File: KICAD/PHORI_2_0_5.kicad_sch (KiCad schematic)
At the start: 110 parts, among them J1 Conn_01x06_Female, J10 Conn_01x01, J2 Conn_01x02, J3 Rumble, J4 Conn_01x02, J5 Conn_01x06, J6 Conn_01x02, J7 USB-C, J8 Conn_01x06, J9 Conn_01x06, Q1 Q_NMOS_GSD, Q2 Q_PMOS_GDS, Q3 Q_NMOS_GSD, SW1 Z, SW10 Dup, SW11 Dright, SW12 Ddown, SW2 A, SW3 B, SW4 X, SW5 Y, SW6 Start, SW7 L, SW8 R, SW9 Dleft, U1 USB-C-24P-QT, U10 MCP3002, U11 MCP3002, U12 Stickbox_Assembly_CStick, U2 RP2040, U3 W25Q128JVS, U4 DRV5055A2xDBZxQ1, U5 DRV5055A2xDBZxQ1, U6 Stickbox_Assembly_Main, U7 AMS1117-3.3, U8 DRV5055A2xDBZxQ1, U9 DRV5055A2xDBZxQ1, Y1 Crystal_GND24

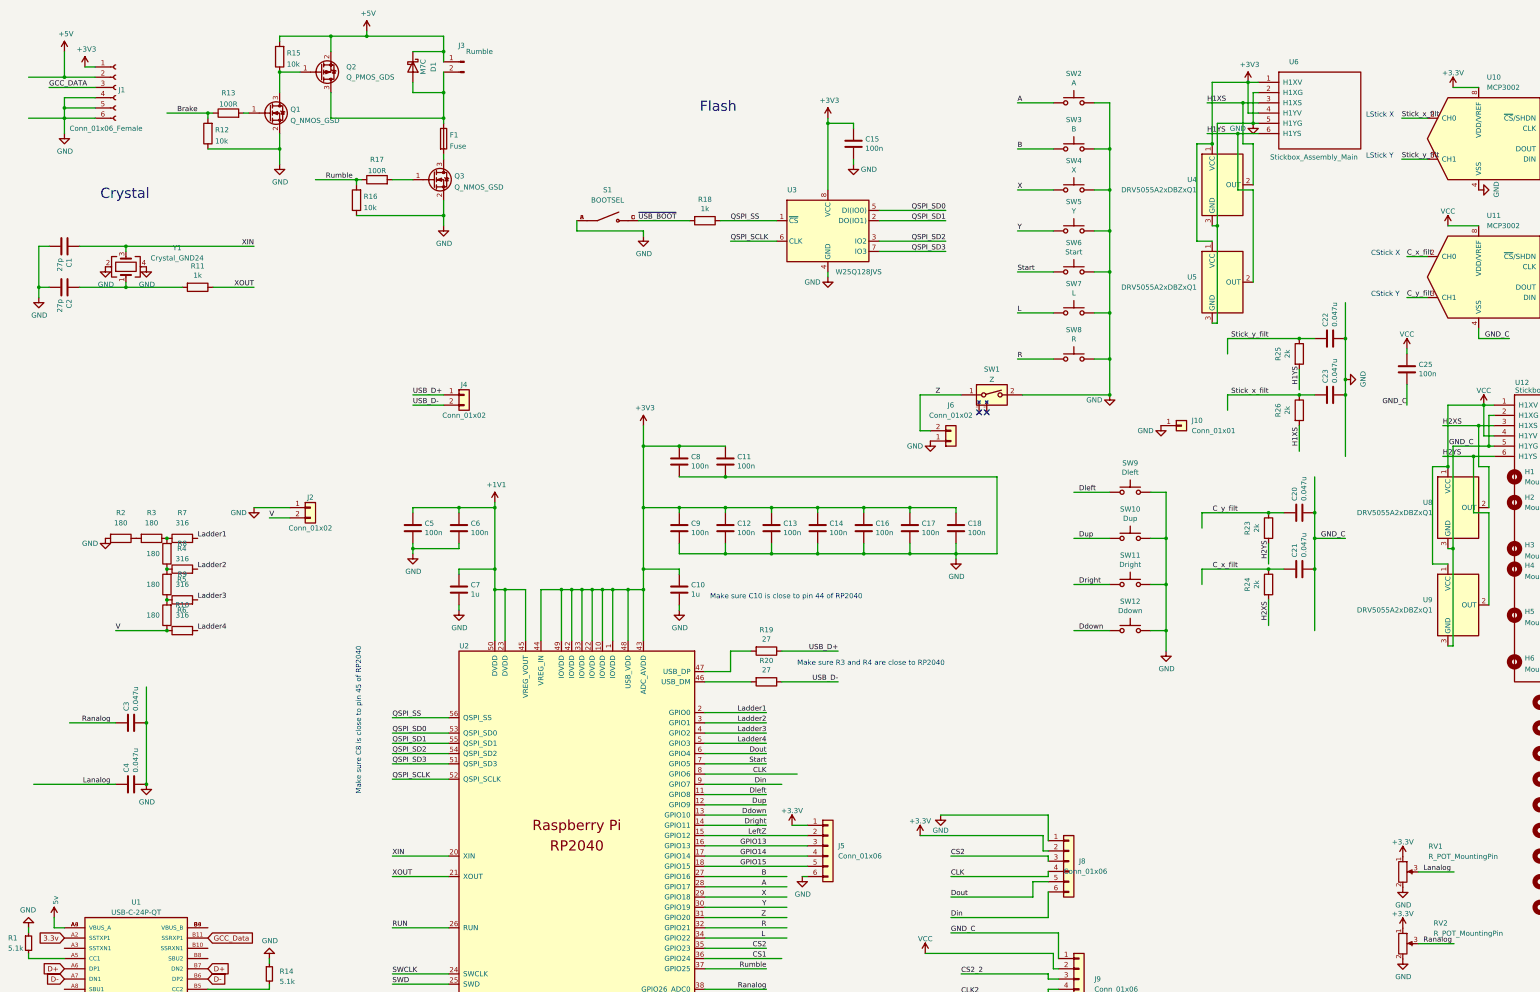
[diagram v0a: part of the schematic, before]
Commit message: GND on Rp2040
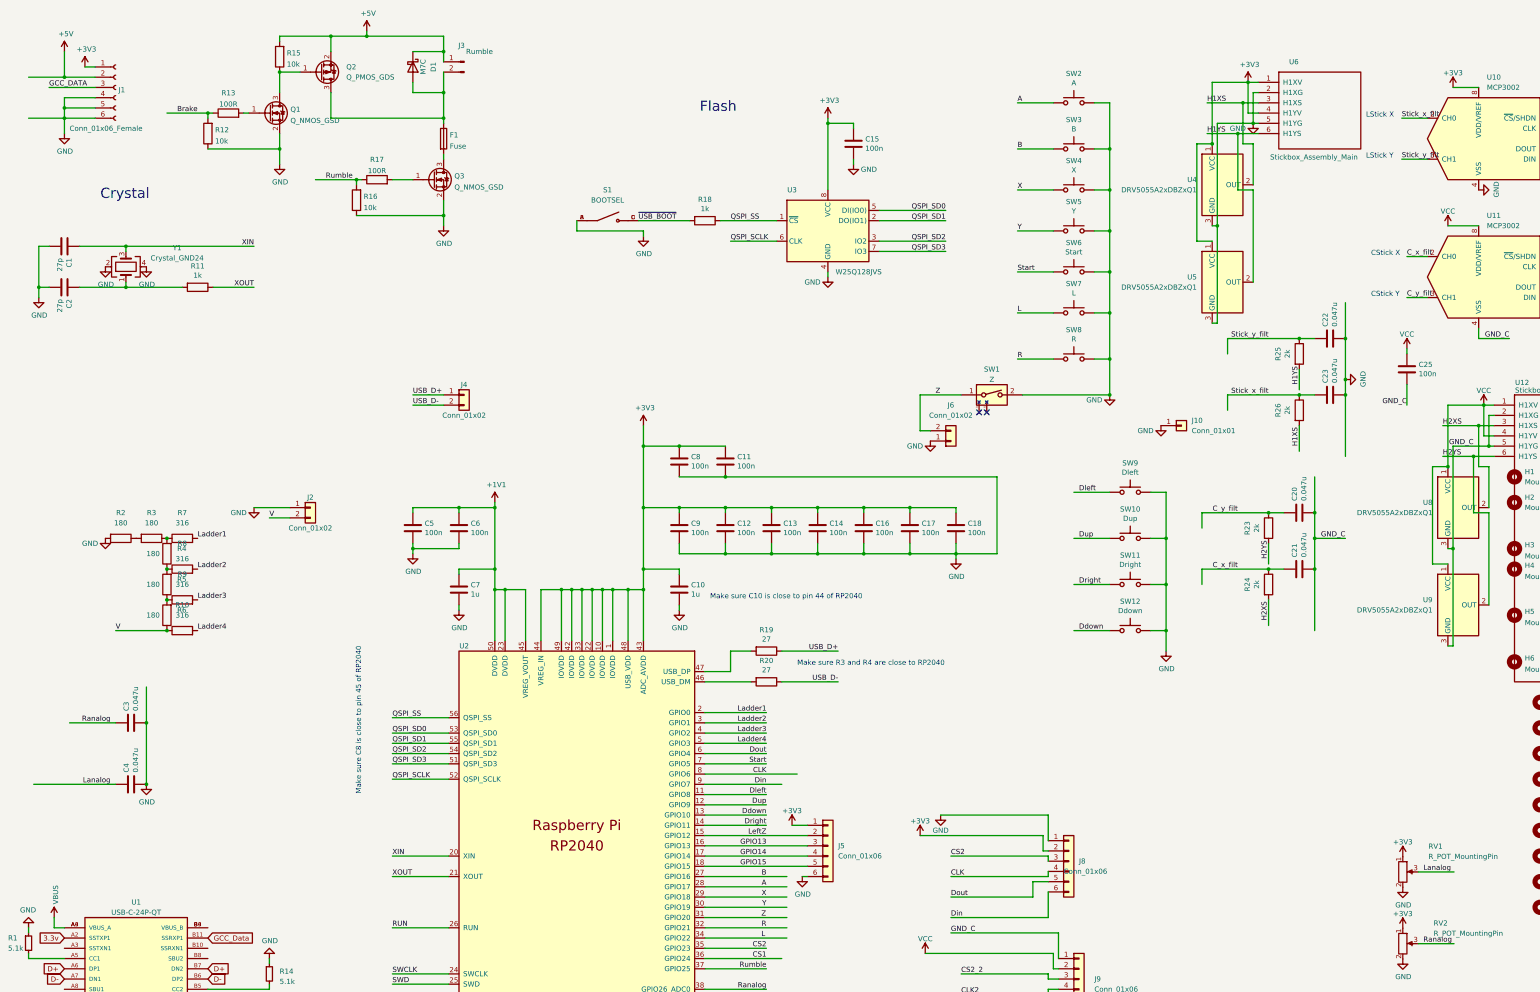
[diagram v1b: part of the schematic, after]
